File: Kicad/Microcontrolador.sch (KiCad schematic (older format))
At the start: 2 parts, among them U1 MSP430G2231IPW14

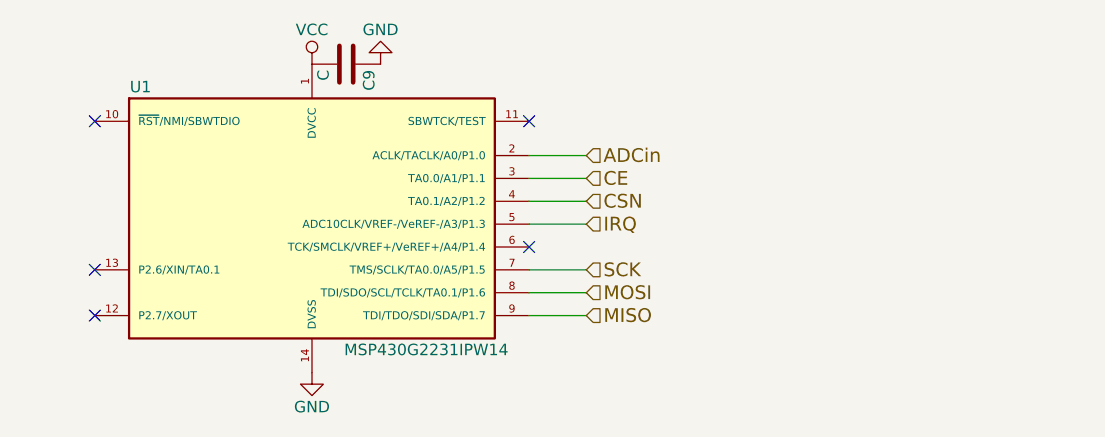
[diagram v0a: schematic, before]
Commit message: Agregado jumpers para programar el micro
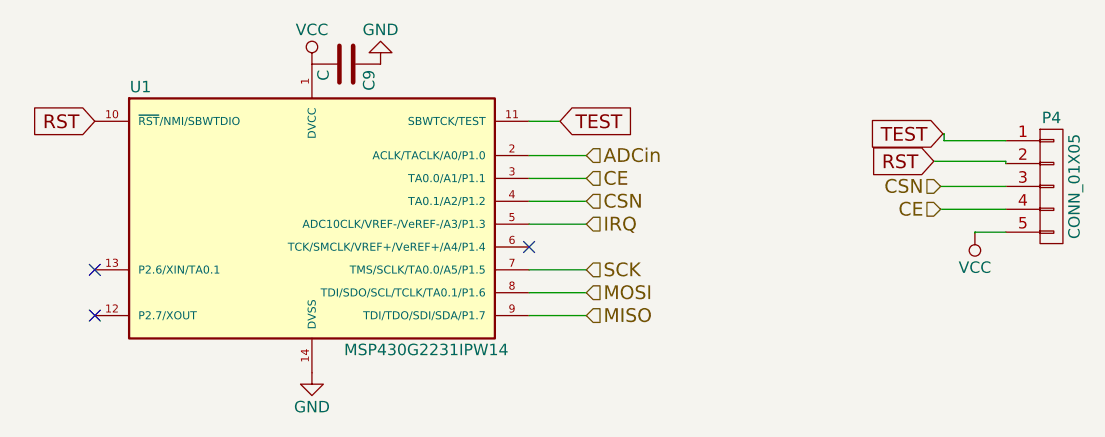
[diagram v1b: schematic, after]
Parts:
- added P4: CONN_01X05, symbol CONN_01X05
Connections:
- net CE: now also P4.4 (P4)
- net CSN: now also P4.3 (P3)
- net VCC: now also P4.5 (P5)
- net RST: now reaches U1.10 (~RST~/NMI/SBWTDIO)
- net RST: now also P4.2 (P2)
- net TEST: now reaches U1.11 (SBWTCK/TEST)
- net TEST: now also P4.1 (P1)
- no-connect marks 5 -> 3
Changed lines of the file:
@@
 	0    1    1    0
 $EndComp
-NoConn ~ 4450 2750
 NoConn ~ 4450 3400
 NoConn ~ 4450 3600
-NoConn ~ 6350 2750
 NoConn ~ 6350 3300
+$Comp
+L CONN_01X05 P4
+U 1 1 58A7015B
+P 8635 3035
+F 0 "P4" H 8635 3335 50  0000 C CNN
+F 1 "CONN_01X05" V 8735 3035 50  0000 C CNN
+F 2 "" H 8635 3035 50  0000 C CNN
+F 3 "" H 8635 3035 50  0000 C CNN
+	1    8635 3035
+	1    0    0    -1
+$EndComp
+Text GLabel 8160 2805 0    60   Input ~ 0
+TEST
+Wire Wire Line
+	8435 2835 8165 2835
+Wire Wire Line
+	8165 2835 8165 2805
+Wire Wire Line
+	8165 2805 8160 2805
+Text GLabel 6485 2750 2    60   Input ~ 0
+TEST
+Wire Wire Line
+	6350 2750 6485 2750
+Text GLabel 8120 2925 0    60   Input ~ 0
+RST
+Text GLabel 4450 2750 0    60   Input ~ 0
+RST
+Wire Wire Line
+	8120 2925 8435 2925
+Wire Wire Line
+	8435 2925 8435 2935
+Text HLabel 8150 3035 0    60   Input ~ 0
+CSN
+Wire Wire Line
+	8435 3035 8150 3035
+Text HLabel 8150 3135 0    60   Input ~ 0
+CE
+$Comp
+L VCC #PWR12
+U 1 1 58A7094B
+P 8300 3240
+F 0 "#PWR12" H 8300 3090 50  0001 C CNN
+F 1 "VCC" H 8300 3390 50  0000 C CNN
+F 2 "" H 8300 3240 50  0000 C CNN
+F 3 "" H 8300 3240 50  0000 C CNN
+	1    8300 3240
+	-1   0    0    1
+$EndComp
+Wire Wire Line
+	8435 3235 8300 3235
+Wire Wire Line
+	8300 3235 8300 3240
+Wire Wire Line
+	8150 3135 8435 3135
 $EndSCHEMATC

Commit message: Agregados footprints de pin headers para elementos faltantes (falta USB)
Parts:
- P4: footprint (none) -> EMG:Pin_Header_Straight_1x05_Pitch2.54mm
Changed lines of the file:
@@
 $EndComp
 $Comp
-L VCC #PWR9
+L VCC #PWR09
 U 1 1 57DD89FE
 P 5400 2500
-F 0 "#PWR9" H 5400 2350 50  0001 C CNN
+F 0 "#PWR09" H 5400 2350 50  0001 C CNN
 F 1 "VCC" H 5400 2650 50  0000 C CNN
 F 2 "" H 5400 2500 50  0000 C CNN
@@
 $EndComp
 $Comp
-L GND #PWR10
+L GND #PWR010
 U 1 1 57DD8A14
 P 5400 3850
-F 0 "#PWR10" H 5400 3600 50  0001 C CNN
+F 0 "#PWR010" H 5400 3600 50  0001 C CNN
 F 1 "GND" H 5400 3700 50  0000 C CNN
 F 2 "" H 5400 3850 50  0000 C CNN
@@
 	6350 3600 6600 3600
 $Comp
-L GND #PWR11
+L GND #PWR011
 U 1 1 57FAAB35
 P 5700 2500
-F 0 "#PWR11" H 5700 2250 50  0001 C CNN
+F 0 "#PWR011" H 5700 2250 50  0001 C CNN
 F 1 "GND" H 5700 2350 50  0000 C CNN
 F 2 "" H 5700 2500 50  0000 C CNN
@@
 F 0 "P4" H 8635 3335 50  0000 C CNN
 F 1 "CONN_01X05" V 8735 3035 50  0000 C CNN
-F 2 "" H 8635 3035 50  0000 C CNN
+F 2 "EMG:Pin_Header_Straight_1x05_Pitch2.54mm" H 8635 3035 50  0001 C CNN
 F 3 "" H 8635 3035 50  0000 C CNN
 	1    8635 3035
@@
 CE
 $Comp
-L VCC #PWR12
+L VCC #PWR012
 U 1 1 58A7094B
 P 8300 3240
-F 0 "#PWR12" H 8300 3090 50  0001 C CNN
+F 0 "#PWR012" H 8300 3090 50  0001 C CNN
 F 1 "VCC" H 8300 3390 50  0000 C CNN
 F 2 "" H 8300 3240 50  0000 C CNN

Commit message: Versión unificada
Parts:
- C9: footprint EMG:C_0805 -> EMG:C_0603
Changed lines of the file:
@@
 F 0 "C9" H 5575 2600 50  0000 L CNN
 F 1 "C" H 5575 2400 50  0000 L CNN
-F 2 "EMG:C_0805" H 5588 2350 50  0001 C CNN
+F 2 "EMG:C_0603" H 5588 2350 50  0001 C CNN
 F 3 "" H 5550 2500 50  0000 C CNN
 	1    5550 2500

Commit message: Cambios en tamaño de pinheaders
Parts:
- P4: footprint EMG:Pin_Header_Straight_1x05_Pitch2.54mm -> EMG:Pin_Header_Straight_1x05_Pitch1.27mm
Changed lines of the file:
@@
 F 0 "P4" H 8635 3335 50  0000 C CNN
 F 1 "CONN_01X05" V 8735 3035 50  0000 C CNN
-F 2 "EMG:Pin_Header_Straight_1x05_Pitch2.54mm" H 8635 3035 50  0001 C CNN
+F 2 "EMG:Pin_Header_Straight_1x05_Pitch1.27mm" H 8635 3035 50  0001 C CNN
 F 3 "" H 8635 3035 50  0000 C CNN
 	1    8635 3035

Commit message: Se agregaron los 3d shapes de el cargador y dc/dc
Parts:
- U1: footprint EMG:TSSOP-14_4.4x5mm_Pitch0.65mm -> EMG:TSSOP-14
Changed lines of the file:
@@
 F 0 "U1" H 4650 3800 50  0000 C CNN
 F 1 "MSP430G2231IPW14" H 5900 2650 50  0000 C CNN
-F 2 "EMG:TSSOP-14_4.4x5mm_Pitch0.65mm" H 4700 2650 50  0001 C CIN
+F 2 "EMG:TSSOP-14" H 4700 2650 50  0001 C CIN
 F 3 "" H 5400 3200 50  0000 C CNN
 	1    5400 3200
